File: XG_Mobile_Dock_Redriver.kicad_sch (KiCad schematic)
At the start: 139 parts, among them J1 5-1775443-8, J13 39301240, J14 I2C1, J2 20455-040E-76, J3 20455-040E-76, J5 USB_C_Receptacle, J6 455860005, J7 10147430-113T0LF, SW1 SW_Push, U1 DS320PR810NJXR, U2 DS320PR810NJXR

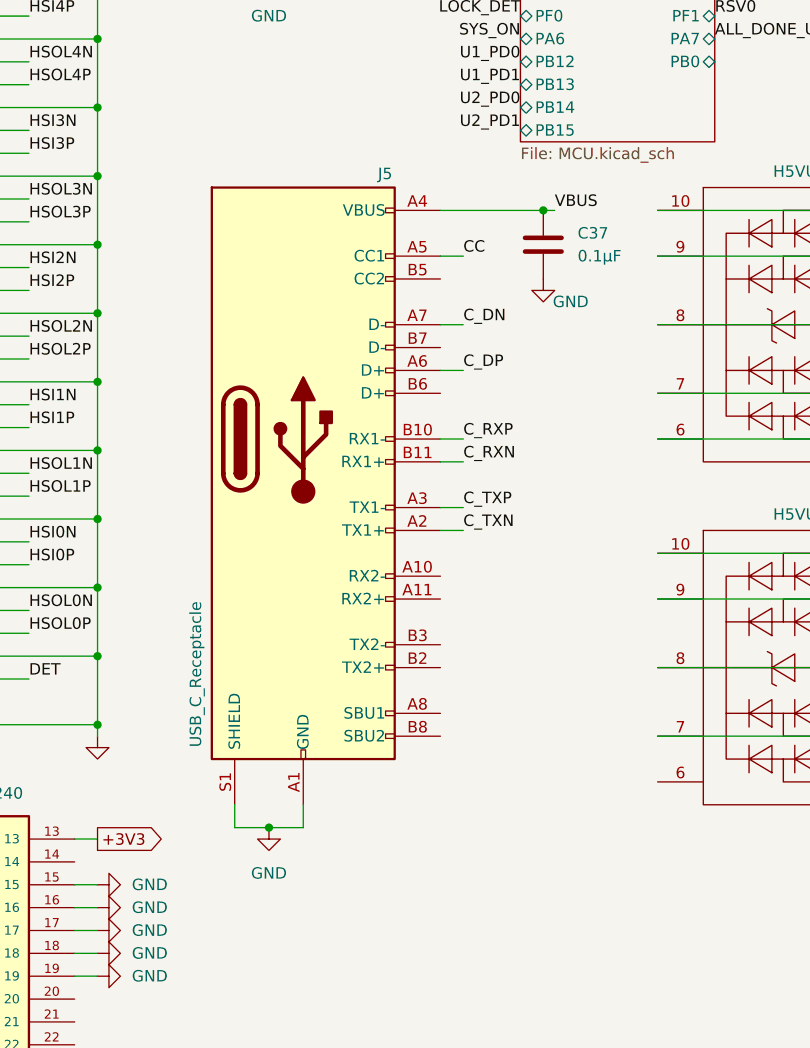
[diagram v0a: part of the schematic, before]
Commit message: new usb c connector
added new usb c connector
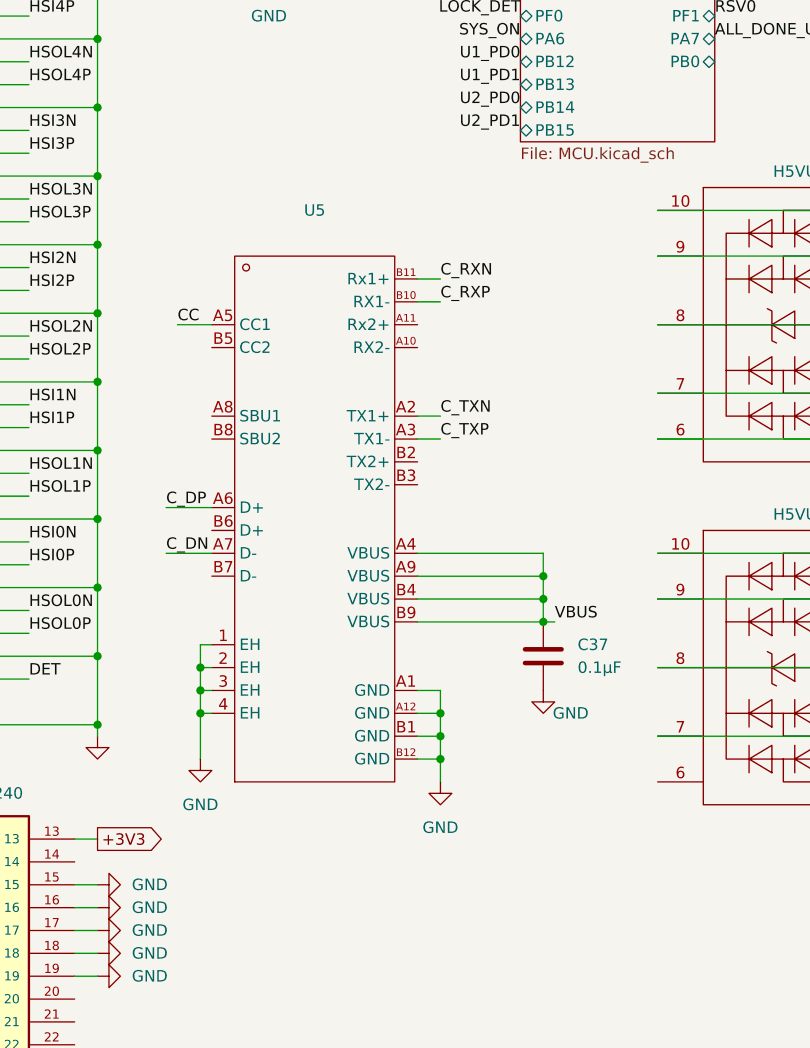
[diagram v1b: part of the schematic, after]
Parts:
- removed J5: USB_C_Receptacle, USB-C-SMD_TYPE-C-24P-QT:USB-C-SMD_TYPE-C-24P-QT, symbol Connector:USB_C_Receptacle
- added U5: ~, GT-USB-7091A:USB-C-SMD_GT-USB-7091A, symbol GT-USB-7091A:GT-USB-7091A
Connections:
- net CC: now also U5.A5 (CC1)
- net C_DN: now also U5.A7 (D-)
- net C_DP: now also U5.A6 (D+)
- net C_RXN: now also U5.B11 (Rx1+)
- net C_RXP: now also U5.B10 (RX1-)
- net C_TXN: now also U5.A2 (TX1+)
- net C_TXP: now also U5.A3 (TX1-)
- net GND: now also U5.1 (EH), U5.2 (EH), U5.3 (EH), U5.4 (EH), U5.A1 (GND), U5.A12 (GND), U5.B1 (GND), U5.B12 (GND)
- net VBUS: now also U5.A4 (VBUS), U5.A9 (VBUS), U5.B4 (VBUS), U5.B9 (VBUS)
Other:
- moved on the sheet: C37

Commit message: added more components
added more components
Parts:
- added U6: ~, LD1085D2T33R:TO-263-2_L10.0-W9.1-P5.08-LS15.2-TL, symbol LD1085D2T33R:LD1085D2T33R
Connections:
- net GND: now also U6.1 (ADJ/GND)
- net +5VSB: now reaches J13.9
- net +5VSB: now also U6.3 (IN)
- new net +3V3SB: U6.4 (OUT)

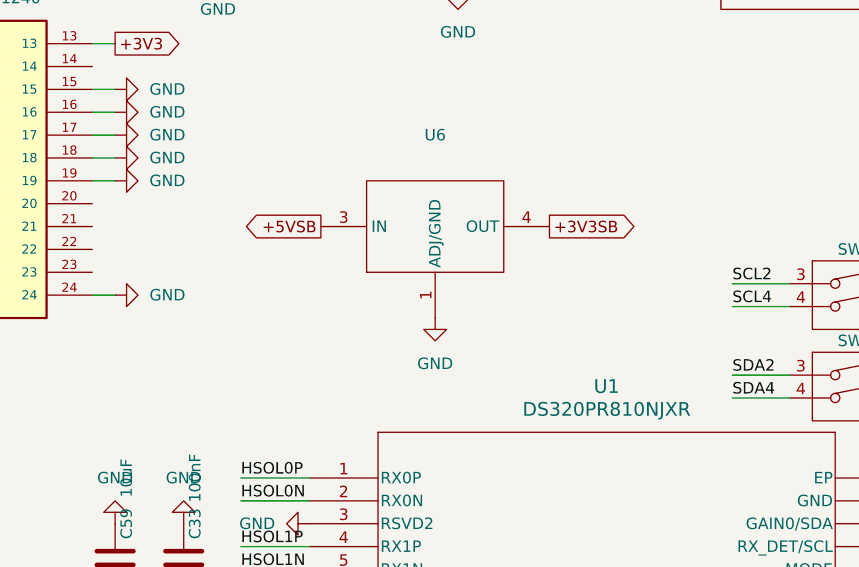
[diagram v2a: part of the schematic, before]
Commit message: added 3v3sb
added 3v3sb
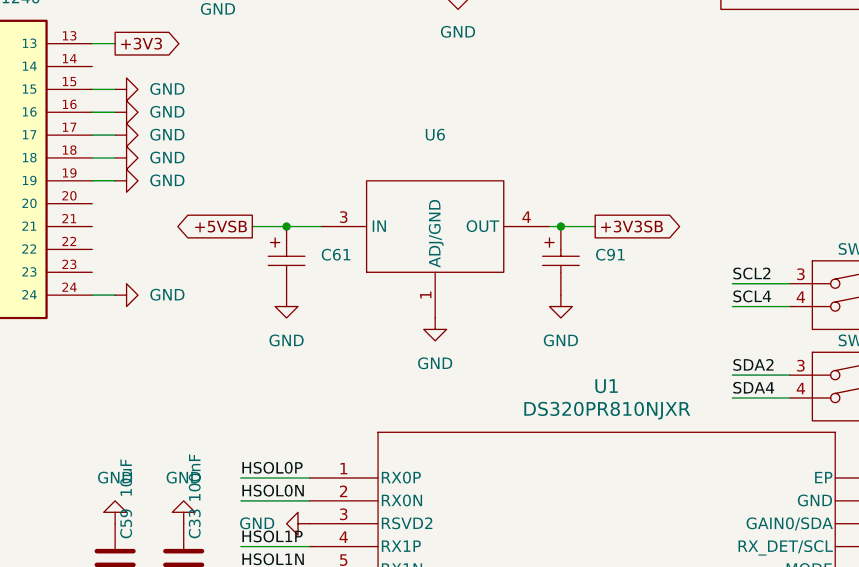
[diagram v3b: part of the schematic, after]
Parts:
- added C61, C91: 10uF, TAJA106K016RNJ:CAP-SMD_L3.2-W1.6-RD-C7171, symbol TAJA106K016RNJ:TAJA106K016RNJ
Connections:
- net +3V3SB: now also C91.1
- net +5VSB: now also C61.1
- net GND: now also C61.2, C91.2

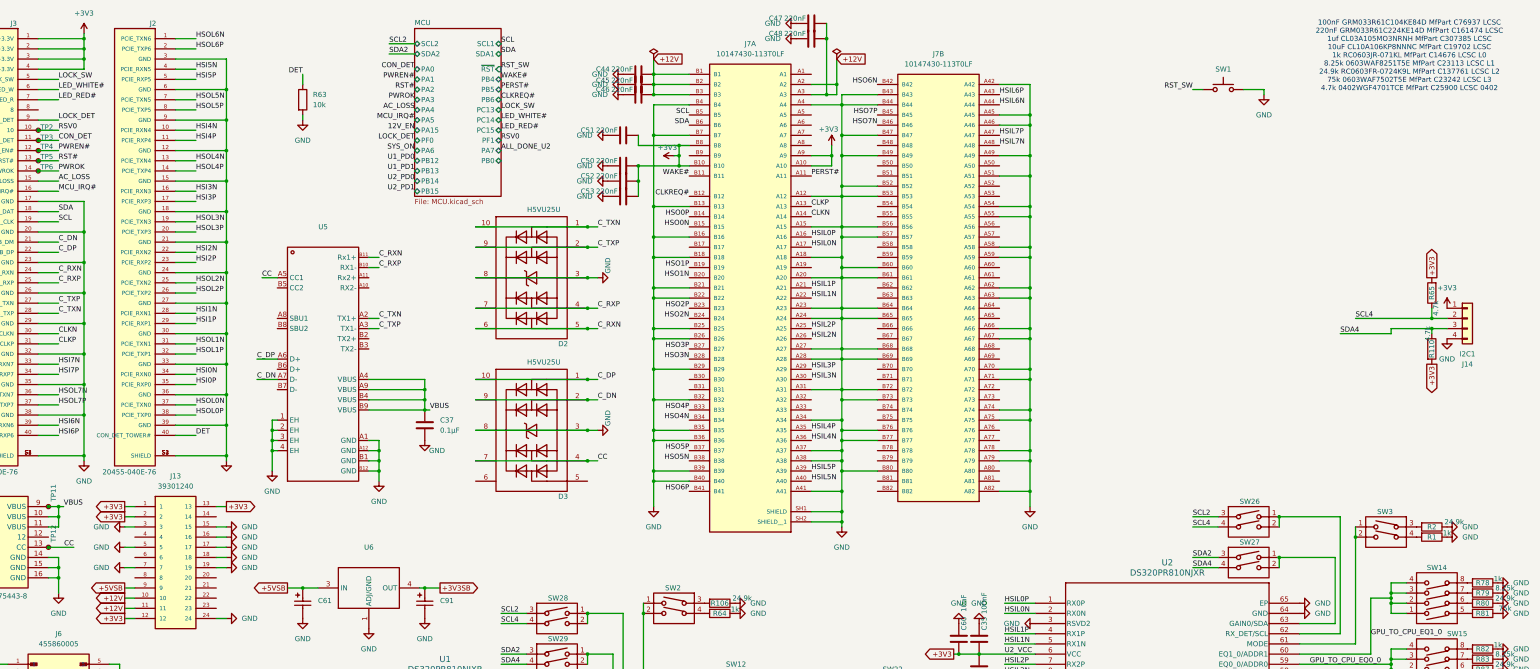
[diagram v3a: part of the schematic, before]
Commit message: added 3v3vsb to mcu
added 3v3vsb to mcu
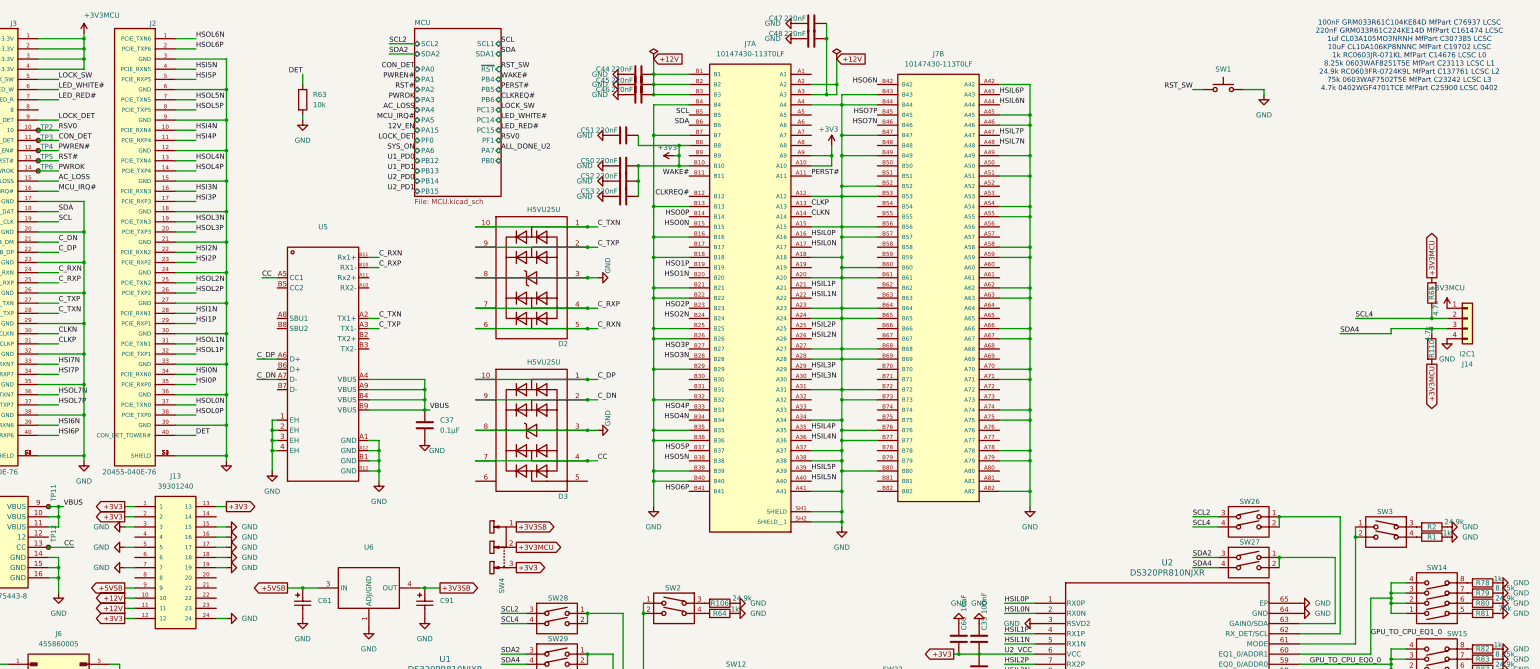
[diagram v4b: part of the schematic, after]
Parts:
- added SW4: ~, SS-12D10L5:SW-TH_SS-12D10L5, symbol SS-12D10L5:SS-12D10L5
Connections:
- net +3V3: now also SW4.3; no longer J14.1 (Pin_1), J3.1 (+3.3V), J3.2 (+3.3V), J3.3 (+3.3V), J3.4 (+3.3V), R110.2, R65.2
- net +3V3SB: now also SW4.1
- new net +3V3MCU: J14.1 (Pin_1), J3.1 (+3.3V), J3.2 (+3.3V), J3.3 (+3.3V), J3.4 (+3.3V), R110.2, R65.2, SW4.2
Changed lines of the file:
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@@
 	(global_label "+3V3"
 		(shape output)
+		(at 154.94 151.13 0)
+		(fields_autoplaced yes)
+		(effects
+			(font
+				(size 1.27 1.27)
+			)
+			(justify left)
+		)
+		(property "Intersheetrefs" "${INTERSHEET_REFS}"
+			(at 163.0052 151.13 0)
+			(effects
+				(font
+					(size 1.27 1.27)
+				)
+				(justify left)
+				(hide yes)
+			)
+		)
+	)
+	(global_label "+3V3"
+		(shape output)
 		(at 82.55 135.89 0)
 		(fields_autoplaced yes)
@@
 		)
 	)
+	(global_label "+3V3MCU"
+		(shape output)
+		(at 154.94 146.05 0)
+		(fields_autoplaced yes)
+		(effects
+			(font
+				(size 1.27 1.27)
+			)
+			(justify left)
+		)
+		(property "Intersheetrefs" "${INTERSHEET_REFS}"
+			(at 167.0571 146.05 0)
+			(effects
+				(font
+					(size 1.27 1.27)
+				)
+				(justify left)
+				(hide yes)
+			)
+		)
+	)
 	(global_label "+5VSB"
 		(shape output)
@@
 		)
 	)
-	(global_label "+3V3"
+	(global_label "+3V3MCU"
 		(shape output)
 		(at 383.54 100.33 270)
@@
 		)
 		(property "Intersheetrefs" "${INTERSHEET_REFS}"
-			(at 383.54 108.3952 90)
+			(at 383.54 112.4471 90)
 			(effects
 				(font
@@
 		)
 	)
-	(global_label "+3V3"
+	(global_label "+3V3MCU"
 		(shape output)
 		(at 383.54 78.74 90)
@@
 		)
 		(property "Intersheetrefs" "${INTERSHEET_REFS}"
-			(at 383.54 70.6748 90)
+			(at 383.54 66.6229 90)
 			(effects
 				(font
@@
 		)
 	)
+	(global_label "+3V3SB"
+		(shape output)
+		(at 154.94 140.97 0)
+		(fields_autoplaced yes)
+		(effects
+			(font
+				(size 1.27 1.27)
+			)
+			(justify left)
+		)
+		(property "Intersheetrefs" "${INTERSHEET_REFS}"
+			(at 165.4847 140.97 0)
+			(effects
+				(font
+					(size 1.27 1.27)
+				)
+				(justify left)
+				(hide yes)
+			)
+		)
+	)
 	(global_label "+3V3"
 		(shape output)
@@
 	)
 	(symbol
+		(lib_id "SS-12D10L5:SS-12D10L5")
+		(at 152.4 146.05 270)
+		(unit 1)
+		(exclude_from_sim no)
+		(in_bom yes)
+		(on_board yes)
+		(dnp no)
+		(fields_autoplaced yes)
+		(property "Reference" "SW4"
+			(at 151.3206 153.67 0)
+			(effects
+				(font
+					(size 1.27 1.27)
+				)
+				(justify left)
+			)
+		)
+		(property "Value" "~"
+			(at 149.4155 153.67 0)
+			(effects
+				(font
+					(size 1.27 1.27)
+				)
+				(justify left)
+			)
+		)
+		(property "Footprint" "SS-12D10L5:SW-TH_SS-12D10L5"
+			(at 152.4 146.05 0)
+			(effects
+				(font
+					(size 1.27 1.27)
+				)
+				(hide yes)
+			)
+		)
+		(property "Datasheet" "https://item.szlcsc.com/datasheet/SS-12D10L5/300104.html"
+			(at 152.4 146.05 0)
+			(effects
+				(font
+					(size 1.27 1.27)
+				)
+				(hide yes)
+			)
+		)
+		(property "Description" "Circuit:SPDT Actuator Style:Rectangular Columnar Termination Style:PC Pin Length:13mm Width:6.8mm Switch Height:6.4mm Mounting Type:Through Hole Actuator Color:Black Current Rating:3A Voltage Rating:125V Life:10,000 Cycles Operating Temperature:-40°C~+85°C"
+			(at 152.4 146.05 0)
+			(effects
+				(font
+					(size 1.27 1.27)
+				)
+				(hide yes)
+			)
+		)
+		(property "Part_Number" "SS-12D10L5"
+			(at 152.4 146.05 0)
+			(effects
+				(font
+					(size 1.27 1.27)
+				)
+				(hide yes)
+			)
+		)
+		(property "Manufacturer" "XKB Connection(中国星坤)"
+			(at 152.4 146.05 0)
+			(effects
+				(font
+					(size 1.27 1.27)
+				)
+				(hide yes)
+			)
+		)
+		(property "LCSC" "C319012"
+			(at 152.4 146.05 0)
+			(effects
+				(font
+					(size 1.27 1.27)
+				)
+				(hide yes)
+			)
+		)
+		(pin "3"
+		)
+		(pin "1"
+		)
+		(pin "2"
+		)
+		(instances
+			(project "XG_Mobile_Dock_Redriver"
+				(path "/f97e6956-ab08-42cb-8fed-03fa58e87f0e"
+					(reference "SW4")
+					(unit 1)
+				)
+			)
+		)
+	)
+	(symbol
 		(lib_id "DSWB02LHGET:DSWB02LHGET")
 		(at 165.1 173.99 270)
@@
 			)
 		)
-		(property "Value" "+3V3"
+		(property "Value" "+3V3MCU"
 			(at 387.35 81.28 0)
 			(effects
@@
 		(on_board yes)
 		(dnp no)
-		(fields_autoplaced yes)
 		(property "Reference" "#PWR0118"
 			(at 46.99 21.59 0)
@@
 			)
 		)
-		(property "Value" "+3V3"
-			(at 46.99 12.7 0)
+		(property "Value" "+3V3MCU"
+			(at 46.99 13.208 0)
 			(effects
 				(font
 					(size 1.27 1.27)
 				)
+				(justify left)
 			)
 		)

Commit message: added ps on
added ps on
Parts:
- added Q1, Q2: ~, MMBT5551 RANGE 200-300:SOT-23-3_L2.9-W1.3-P1.90-LS2.4-BR, symbol MMBT5551(RANGE_200-300):MMBT5551_C2145
- added R111: 4k, Resistor_SMD:R_0603_1608Metric, symbol Device:R
- added R113: 100k, Resistor_SMD:R_0603_1608Metric, symbol Device:R
- added R114: 470k, Resistor_SMD:R_0603_1608Metric, symbol Device:R
- added R115: 10k, Resistor_SMD:R_0603_1608Metric, symbol Device:R
- added SW30: ~, DSWB02LHGET:SW-TH_DSWB02LHGET, symbol DSWB02LHGET:DSWB02LHGET
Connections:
- net +3V3MCU: now also R115.1
- net GND: now also Q1.2 (E), Q2.2 (E), R114.2, SW30.4; no longer J13.16
- net PSPWROK: now reaches J13.8
- net PSPWROK: now also R113.1
- new net: Q1.1 (B), R111.2
- new net: Q1.3 (C), SW30.3
- new net: J13.16, SW30.1, SW30.2
- new net: Q2.1 (B), R113.2, R114.1
- new net PSON: R111.1
- new net PSPWROK3V3: Q2.3 (C), R115.2
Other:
- sheet MCU ports: added PB2; removed none
- moved on the sheet: C61, C91, U6

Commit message: Update XG_Mobile_Dock_Redriver.kicad_sch
added schematic
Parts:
- added FB1, FB2: FerriteBead, Resistor_SMD:R_1206_3216Metric, symbol Device:FerriteBead
- added SW5, SW8: ~, SS-12D10L5:SW-TH_SS-12D10L5, symbol SS-12D10L5:SS-12D10L5
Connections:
- net +3V3: now also FB1.2; no longer C33.2, C34.2, C35.2, C36.2, C38.2, C39.2, C40.2, C41.2, C42.2, C43.2, C49.2, C54.2, C55.2, C56.2, C57.2, C58.2, C59.2, C60.2, SW20.4, SW21.4, SW22.4, SW23.4, U1.18 (VCC), U1.38 (VCC), U1.50 (VCC), U1.6 (VCC), U2.18 (VCC), U2.38 (VCC), U2.50 (VCC), U2.6 (VCC)
- net +3V3SB: now also FB2.2
- new net: FB2.1, SW5.1
- new net: FB1.1, SW8.1
- new net +3V3Redriver: C33.2, C34.2, C35.2, C36.2, C38.2, C39.2, C40.2, C41.2, C42.2, C43.2, C49.2, C54.2, C55.2, C56.2, C57.2, C58.2, C59.2, C60.2, SW20.4, SW21.4, SW22.4, SW23.4, SW5.2, SW8.2, U1.18 (VCC), U1.38 (VCC), U1.50 (VCC), U1.6 (VCC), U2.18 (VCC), U2.38 (VCC), U2.50 (VCC), U2.6 (VCC)

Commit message: more tweaks
more tweaks
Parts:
- U6: LCSC (none) -> C7913; LCSC Part Name 3 A低压降可调和固定正电压稳压器 -> (none); Manufacturer Part LD1085D2T33R -> (none); Part_Number (none) -> LD1085D2T33R; Supplier LCSC -> (none); Supplier Part C7913 -> (none)
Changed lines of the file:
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@@
 			)
 		)
-		(property "Manufacturer Part" "LD1085D2T33R"
+		(property "Part_Number" "LD1085D2T33R"
 			(at 330.2 55.88 0)
 			(effects
@@
 			)
 		)
-		(property "Supplier Part" "C7913"
+		(property "LCSC" "C7913"
 			(at 330.2 55.88 0)
 			(effects
-				(font
-					(size 1.27 1.27)
-				)
-				(hide yes)
-			)
-		)
-		(property "Supplier" "LCSC"
-			(at 330.2 55.88 0)
-			(effects
-				(font
-					(size 1.27 1.27)
-				)
-				(hide yes)
-			)
-		)
-		(property "LCSC Part Name" "3 A低压降可调和固定正电压稳压器"
-			(at 330.2 55.88 0)
-			(effects

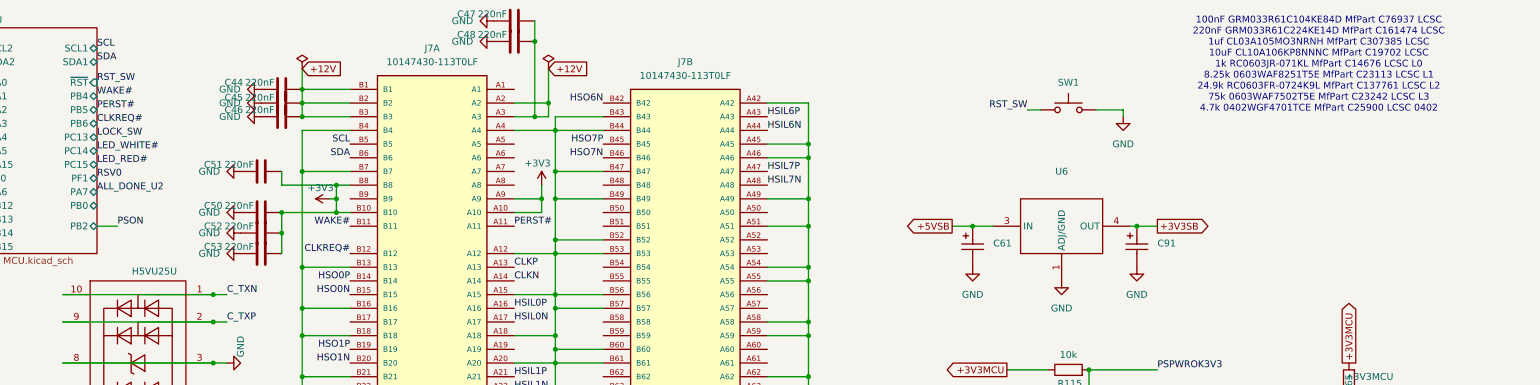
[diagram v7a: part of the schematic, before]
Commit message: added separate perst pull up and transistor for level translation
added separate perst pull up and transistor for level translation
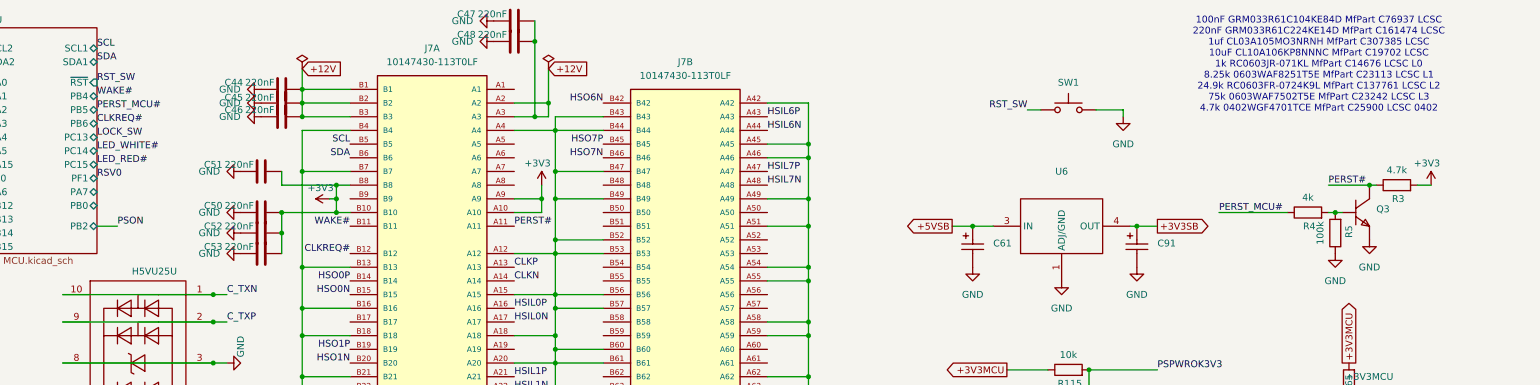
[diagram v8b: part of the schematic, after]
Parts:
- added Q3: ~, MMBT5551 RANGE 200-300:SOT-23-3_L2.9-W1.3-P1.90-LS2.4-BR, symbol MMBT5551(RANGE_200-300):MMBT5551_C2145
- added R3: 4.7k, Resistor_SMD:R_0402_1005Metric, symbol Device:R
- added R4: 4k, Resistor_SMD:R_0603_1608Metric, symbol Device:R
- added R5: 100k, Resistor_SMD:R_0603_1608Metric, symbol Device:R
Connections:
- net +3V3: now also R3.2
- net GND: now also Q3.2 (E), R5.1
- net PERST#: now also Q3.3 (C), R3.1
- new net: Q3.1 (B), R4.2, R5.2
- new net PERST_MCU#: R4.1
